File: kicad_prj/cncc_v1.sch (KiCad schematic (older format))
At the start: 0 parts

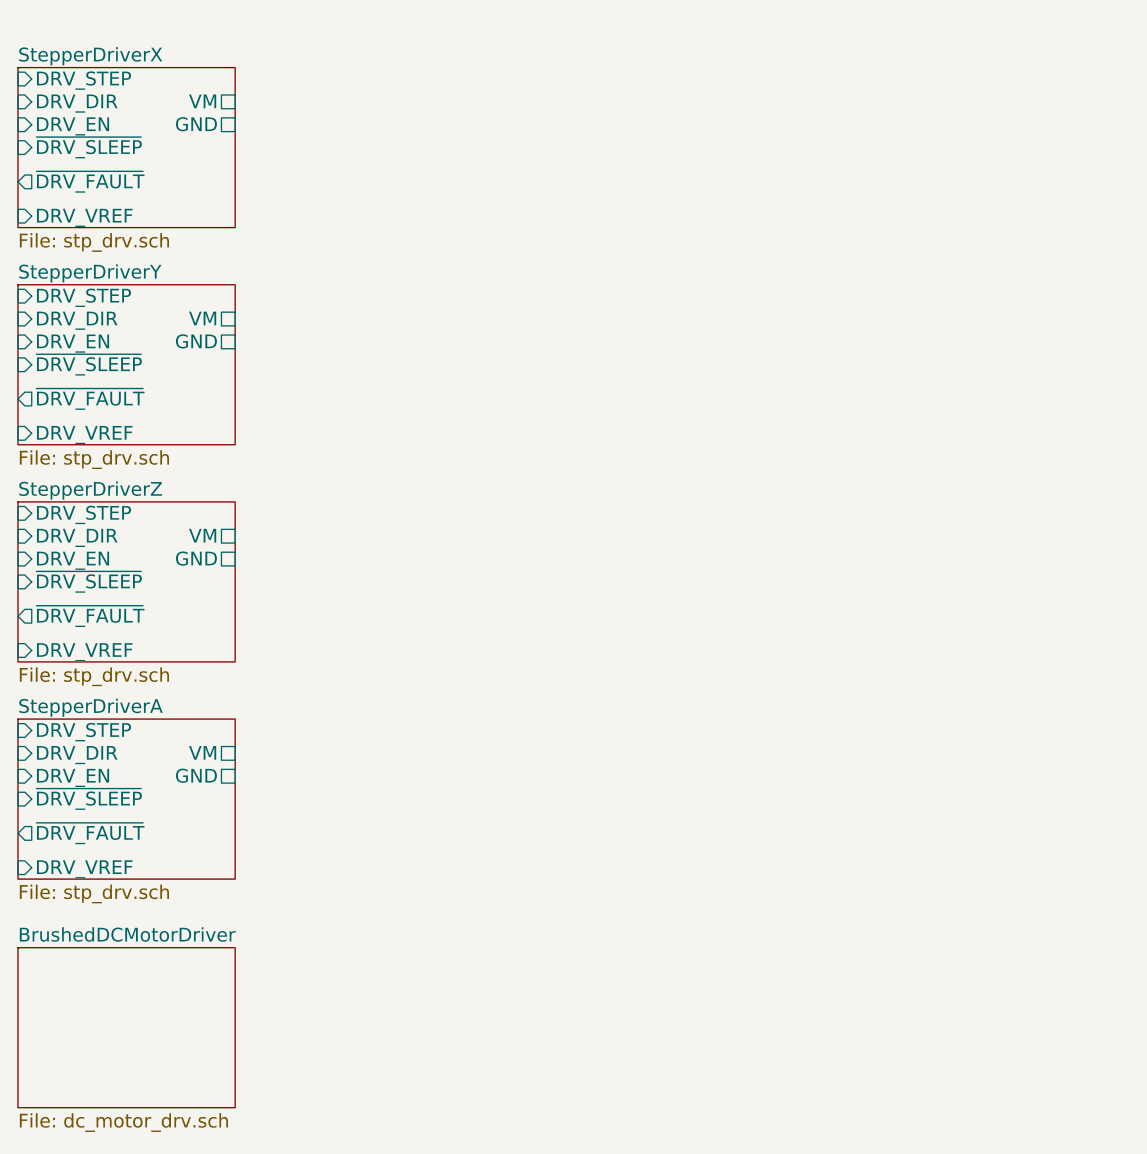
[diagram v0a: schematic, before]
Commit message: Schematics 3
Added spindle driver and sensors/limit switches.
Need to add terminals for ADC channels.
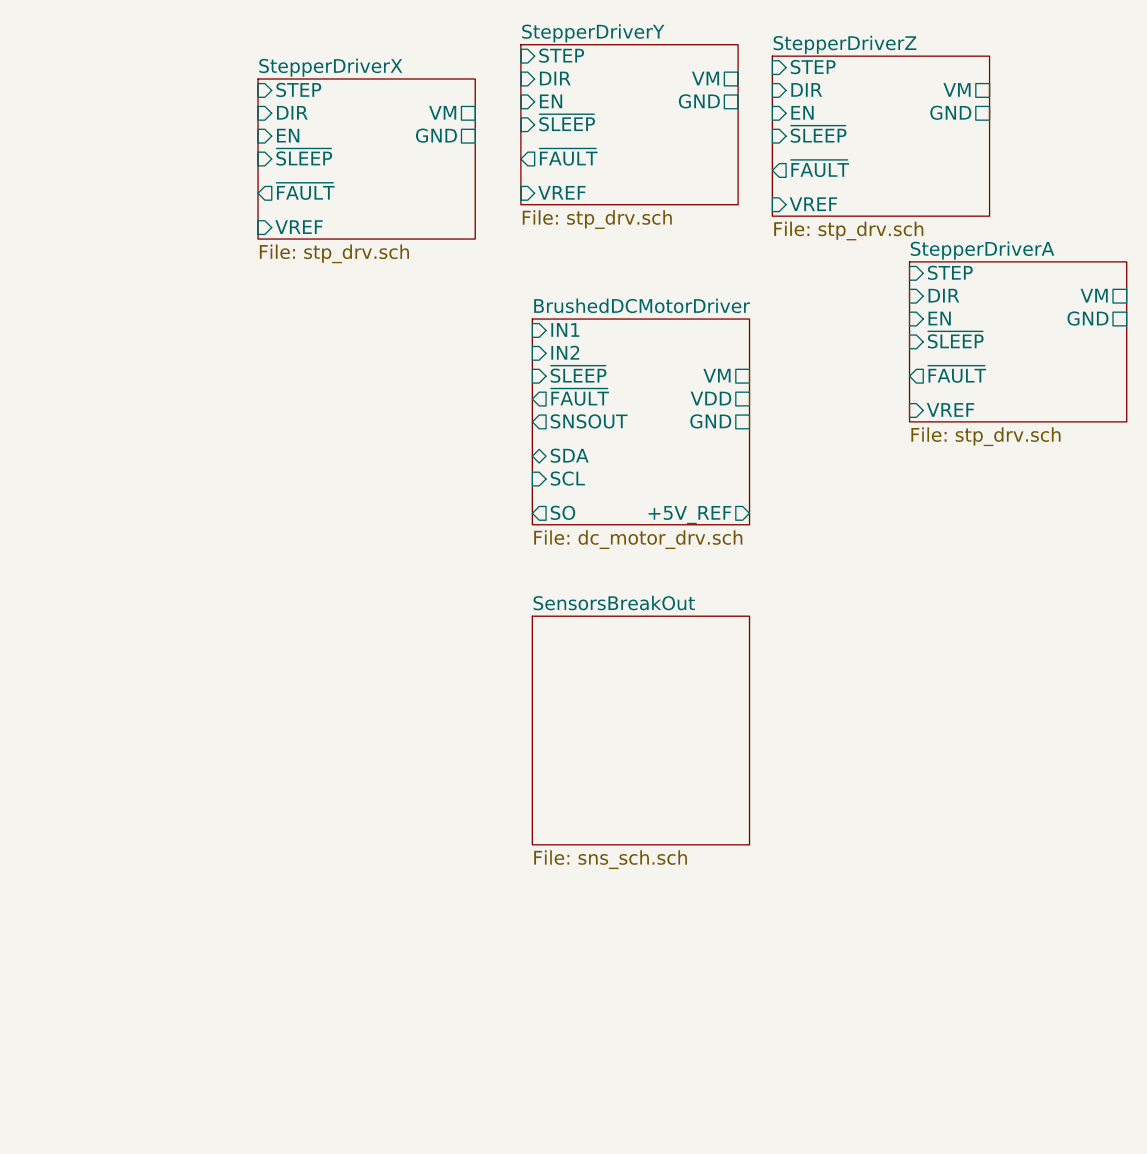
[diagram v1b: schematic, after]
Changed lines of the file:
@@
 $Descr A 11000 8500
 encoding utf-8
-Sheet 1 6
+Sheet 1 7
 Title ""
 Date ""
@@
 $EndDescr
 $Sheet
-S 5500 750  950  700
+S 6550 800  950  700
 U 56526EA5
 F0 "StepperDriverX" 60
 F1 "stp_drv.sch" 60
-F2 "DRV_STEP" I L 5500 800 60
-F3 "DRV_DIR" I L 5500 900 60
-F4 "DRV_EN" I L 5500 1000 60
-F5 "~DRV_SLEEP" I L 5500 1100 60
-F6 "DRV_VREF" I L 5500 1400 60
-F7 "~DRV_FAULT" O L 5500 1250 60
-F8 "VM" U R 6450 900 60
-F9 "GND" U R 6450 1000 60
+F2 "VM" U R 7500 950 60
+F3 "GND" U R 7500 1050 60
+F4 "STEP" I L 6550 850 60
+F5 "DIR" I L 6550 950 60
+F6 "EN" I L 6550 1050 60
+F7 "~SLEEP" I L 6550 1150 60
+F8 "VREF" I L 6550 1450 60
+F9 "~FAULT" O L 6550 1300 60
 $EndSheet
 $Sheet
-S 5500 1700 950  700
+S 7700 650  950  700
 U 5653D417
 F0 "StepperDriverY" 60
 F1 "stp_drv.sch" 60
-F2 "DRV_STEP" I L 5500 1750 60
-F3 "DRV_DIR" I L 5500 1850 60
-F4 "DRV_EN" I L 5500 1950 60
-F5 "~DRV_SLEEP" I L 5500 2050 60
-F6 "DRV_VREF" I L 5500 2350 60
-F7 "~DRV_FAULT" O L 5500 2200 60
-F8 "VM" U R 6450 1850 60
-F9 "GND" U R 6450 1950 60
+F2 "VM" U R 8650 800 60
+F3 "GND" U R 8650 900 60
+F4 "STEP" I L 7700 700 60
+F5 "DIR" I L 7700 800 60
+F6 "EN" I L 7700 900 60
+F7 "~SLEEP" I L 7700 1000 60
+F8 "VREF" I L 7700 1300 60
+F9 "~FAULT" O L 7700 1150 60
 $EndSheet
 $Sheet
-S 5500 2650 950  700
+S 8800 700  950  700
 U 56542384
 F0 "StepperDriverZ" 60
 F1 "stp_drv.sch" 60
-F2 "DRV_STEP" I L 5500 2700 60
-F3 "DRV_DIR" I L 5500 2800 60
-F4 "DRV_EN" I L 5500 2900 60
-F5 "~DRV_SLEEP" I L 5500 3000 60
-F6 "DRV_VREF" I L 5500 3300 60
-F7 "~DRV_FAULT" O L 5500 3150 60
-F8 "VM" U R 6450 2800 60
-F9 "GND" U R 6450 2900 60
+F2 "VM" U R 9750 850 60
+F3 "GND" U R 9750 950 60
+F4 "STEP" I L 8800 750 60
+F5 "DIR" I L 8800 850 60
+F6 "EN" I L 8800 950 60
+F7 "~SLEEP" I L 8800 1050 60
+F8 "VREF" I L 8800 1350 60
+F9 "~FAULT" O L 8800 1200 60
 $EndSheet
 $Sheet
-S 5500 3600 950  700
+S 9400 1600 950  700
 U 5654C1EE
 F0 "StepperDriverA" 60
 F1 "stp_drv.sch" 60
-F2 "DRV_STEP" I L 5500 3650 60
-F3 "DRV_DIR" I L 5500 3750 60
-F4 "DRV_EN" I L 5500 3850 60
-F5 "~DRV_SLEEP" I L 5500 3950 60
-F6 "DRV_VREF" I L 5500 4250 60
-F7 "~DRV_FAULT" O L 5500 4100 60
-F8 "VM" U R 6450 3750 60
-F9 "GND" U R 6450 3850 60
+F2 "VM" U R 10350 1750 60
+F3 "GND" U R 10350 1850 60
+F4 "STEP" I L 9400 1650 60
+F5 "DIR" I L 9400 1750 60
+F6 "EN" I L 9400 1850 60
+F7 "~SLEEP" I L 9400 1950 60
+F8 "VREF" I L 9400 2250 60
+F9 "~FAULT" O L 9400 2100 60
 $EndSheet
 $Sheet
-S 5500 4600 950  700
+S 7750 1850 950  900
 U 5653A94A
 F0 "BrushedDCMotorDriver" 60
 F1 "dc_motor_drv.sch" 60
+F2 "IN1" I L 7750 1900 60
+F3 "IN2" I L 7750 2000 60
+F4 "~SLEEP" I L 7750 2100 60
+F5 "~FAULT" O L 7750 2200 60
+F6 "SNSOUT" O L 7750 2300 60
+F7 "SDA" B L 7750 2450 60
+F8 "SCL" I L 7750 2550 60
+F9 "VM" U R 8700 2100 60
+F10 "VDD" U R 8700 2200 60
+F11 "GND" U R 8700 2300 60
+F12 "SO" O L 7750 2700 60
+F13 "+5V_REF" O R 8700 2700 60
+$EndSheet
+$Sheet
+S 7750 3150 950  1000
+U 5659B5AB
+F0 "SensorsBreakOut" 60
+F1 "sns_sch.sch" 60
 $EndSheet
 $EndSCHEMATC

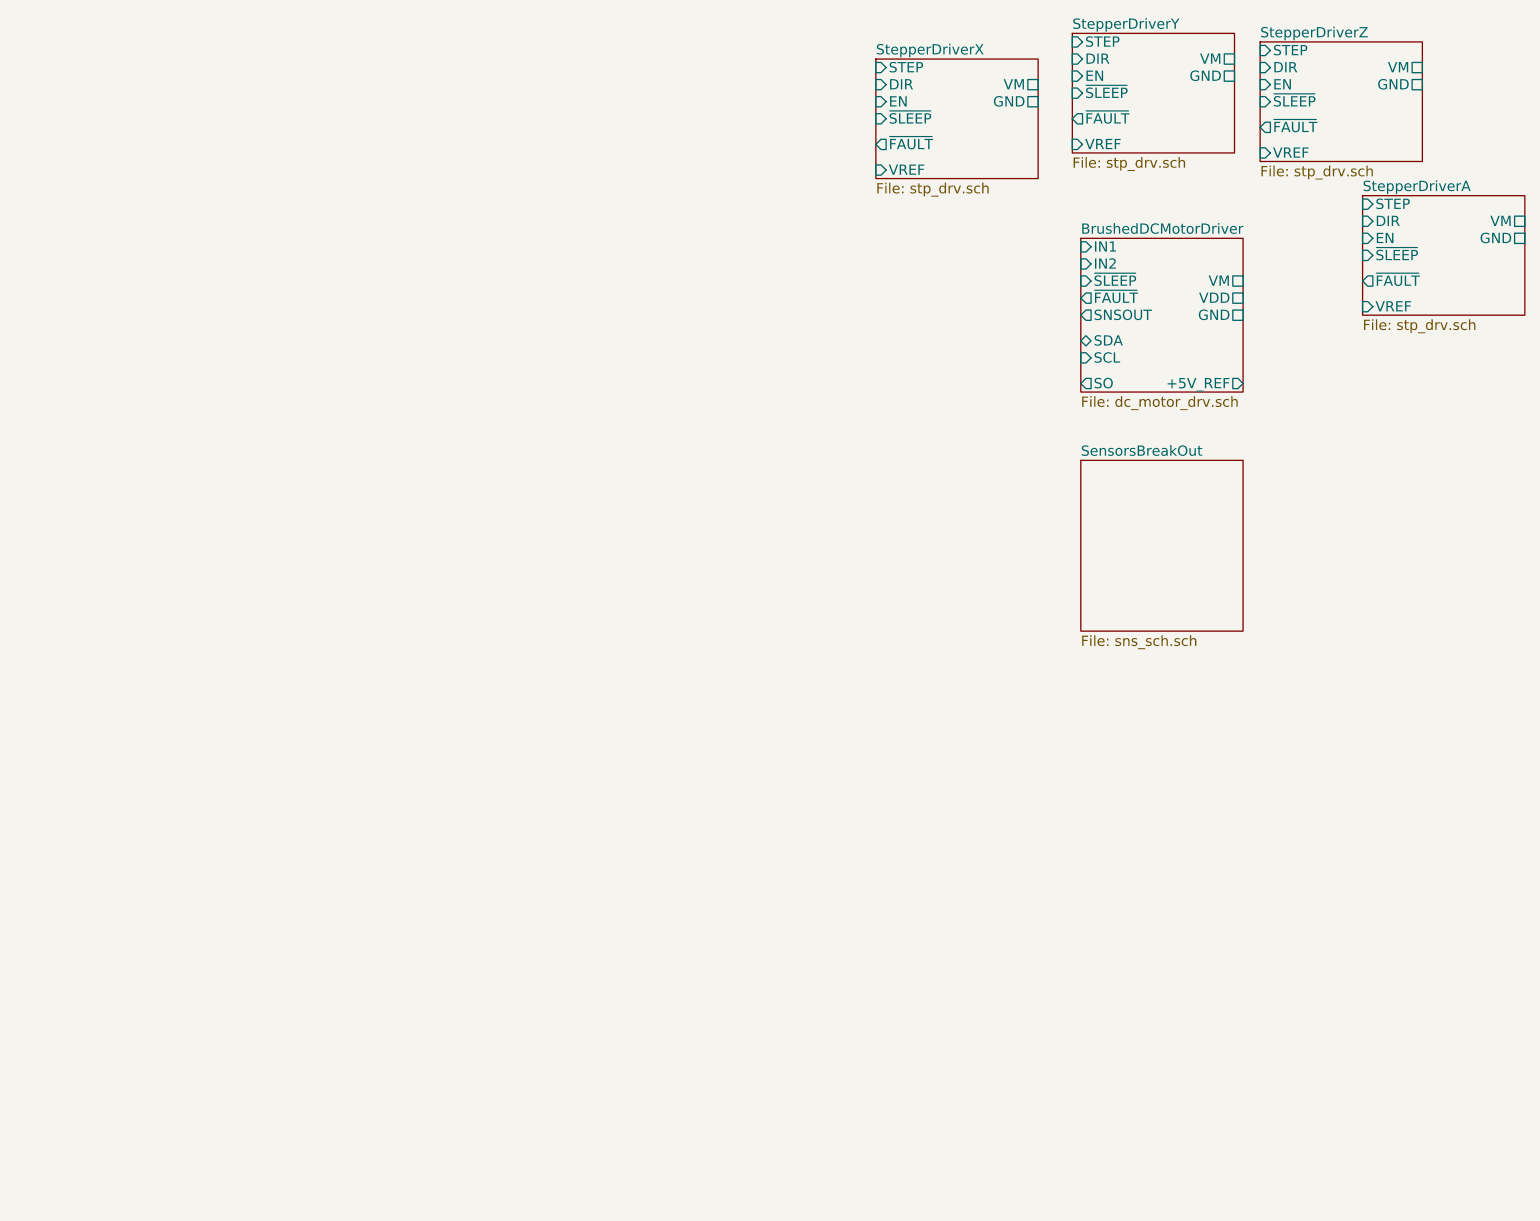
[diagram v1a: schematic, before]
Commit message: Schematics 4
Finished sensor inputs.
Added DAC for stepper motor drivers.
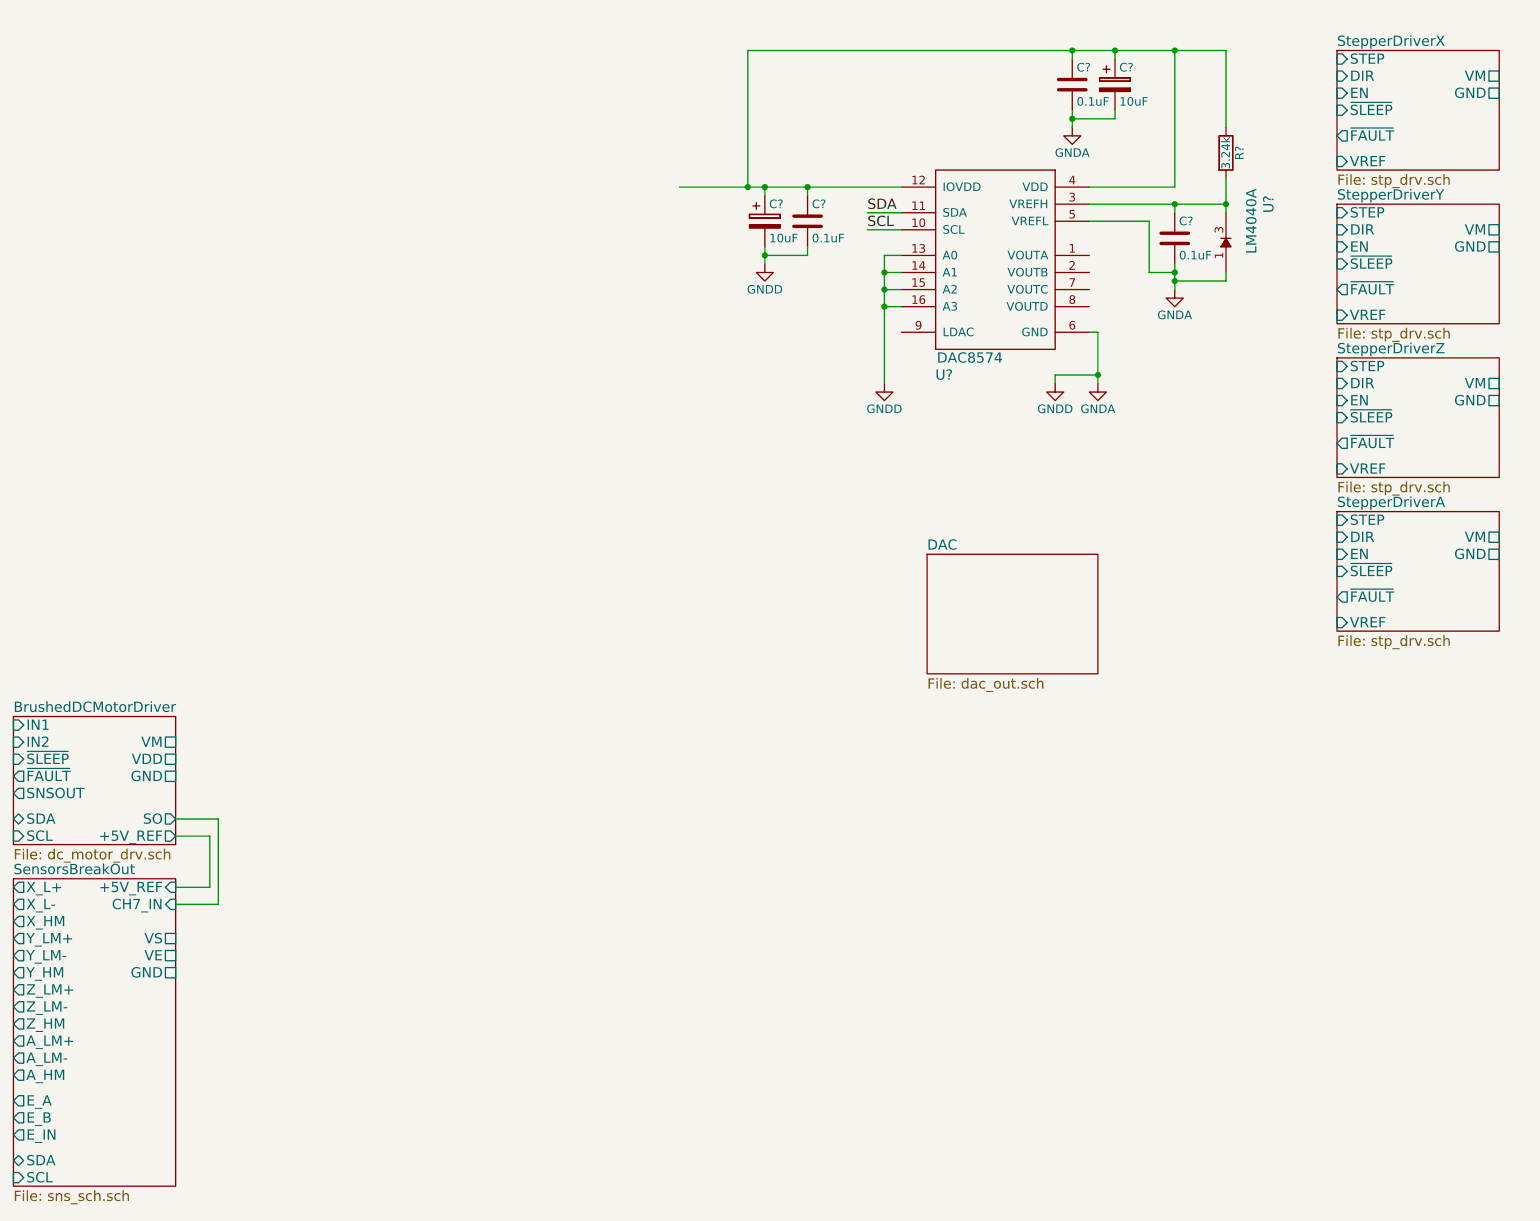
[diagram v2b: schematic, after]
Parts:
- added C? (x2): 10uF, symbol CP
- added C? (x3): 0.1uF, symbol C
- added R?: 3.24k, symbol R
- added U?: DAC8574, symbol DAC8574
- added U?: LM4040A, symbol LM4040A
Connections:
- new net: C?.1, C?.1, C?.1, C?.1, R?.1, U?.12 (IOVDD), U?.4 (VDD), U?.5 (NC)
- new net: C?.1, R?.2, U?.3, U?.3 (VREFH)
- new net GNDA: C?.2, C?.2, C?.2, C?.2, C?.2, U?.1, U?.13 (A0), U?.14 (A1), U?.15 (A2), U?.16 (A3), U?.5 (VREFL), U?.6 (GND)
- new net SCL: U?.10 (SCL)
- new net SDA: U?.11 (SDA)

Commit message: Schematics 5
Started isolation part.
Selected ICs for SPI isolation and general digital I/Os.
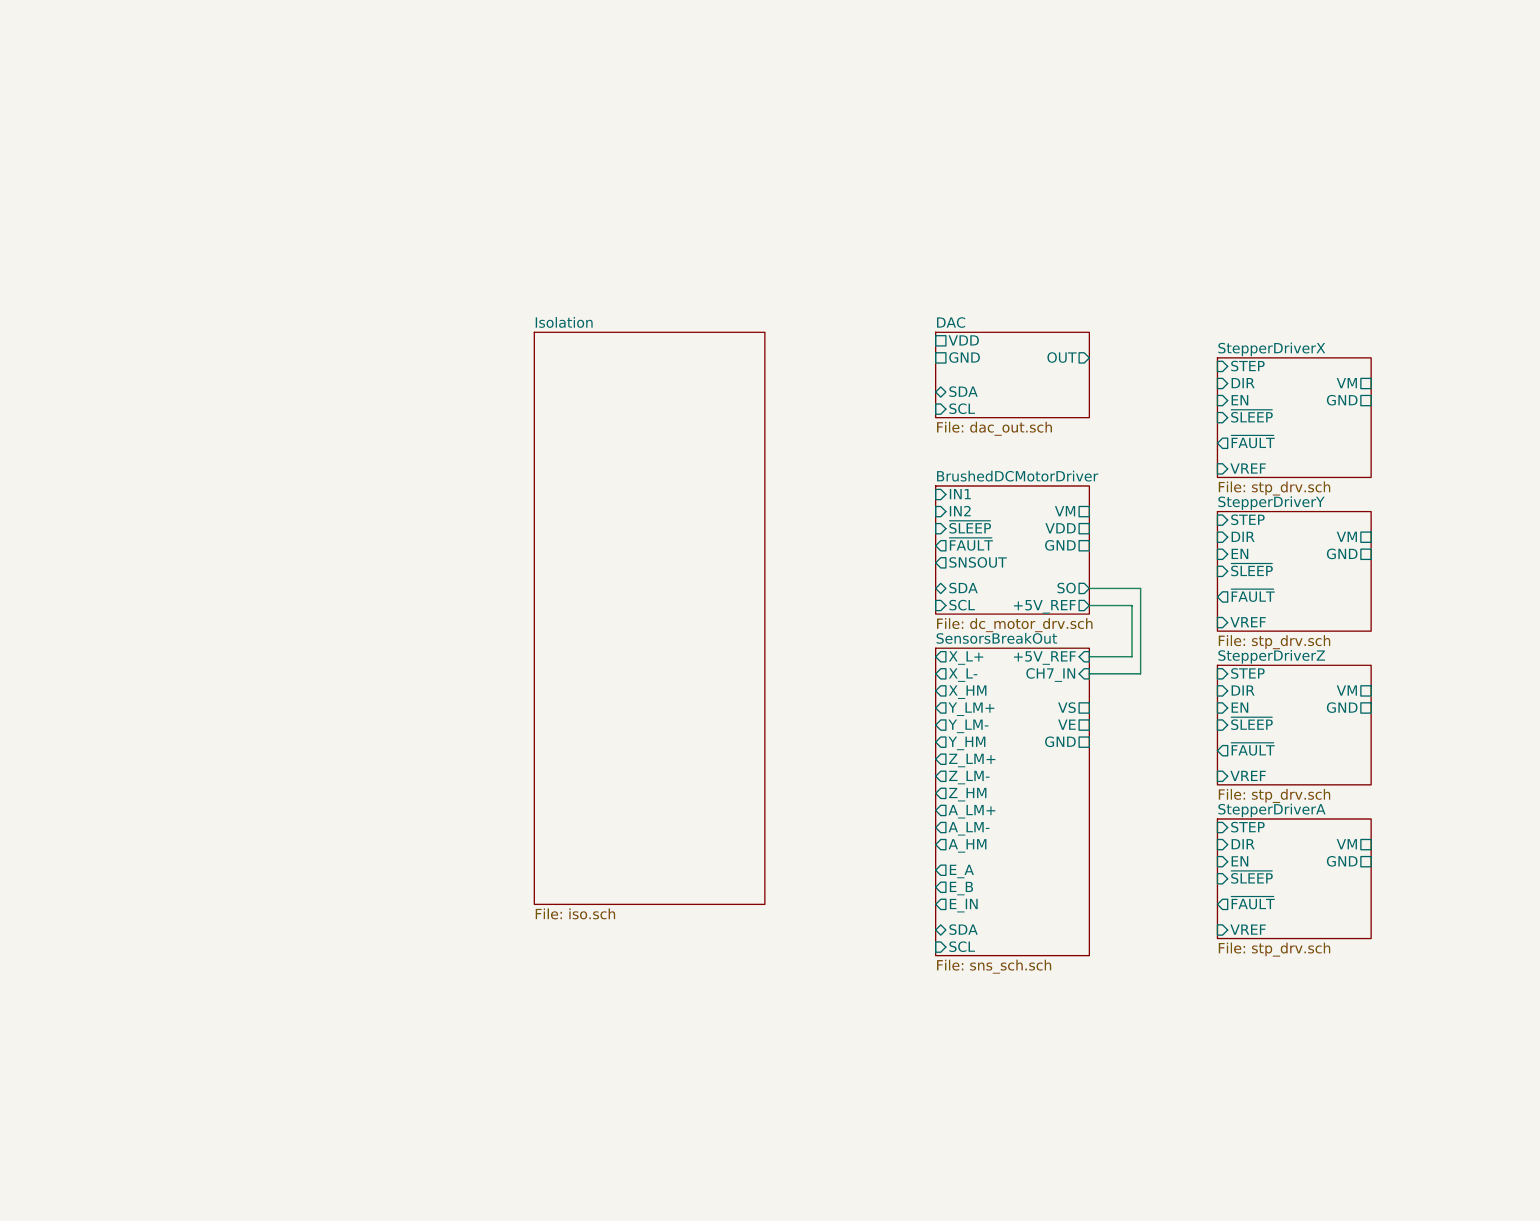
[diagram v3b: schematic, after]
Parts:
- removed C? (x2): 10uF, symbol CP
- removed C? (x3): 0.1uF, symbol C
- removed R?: 3.24k, symbol R
- removed U?: DAC8574, symbol DAC8574
- removed U?: LM4040A, symbol LM4040A
